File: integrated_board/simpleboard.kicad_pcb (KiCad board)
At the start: 4 copper layers, 50 x 50 mm, 111 parts, among them IC1 MPM36xx, IC2 IP4251, J1 OLED, J2 SERIAL1, J3 USB_B_Micro, J4 Battery, J6 Battery, J8 FAN, J9 Enc, P1 SWD_TC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

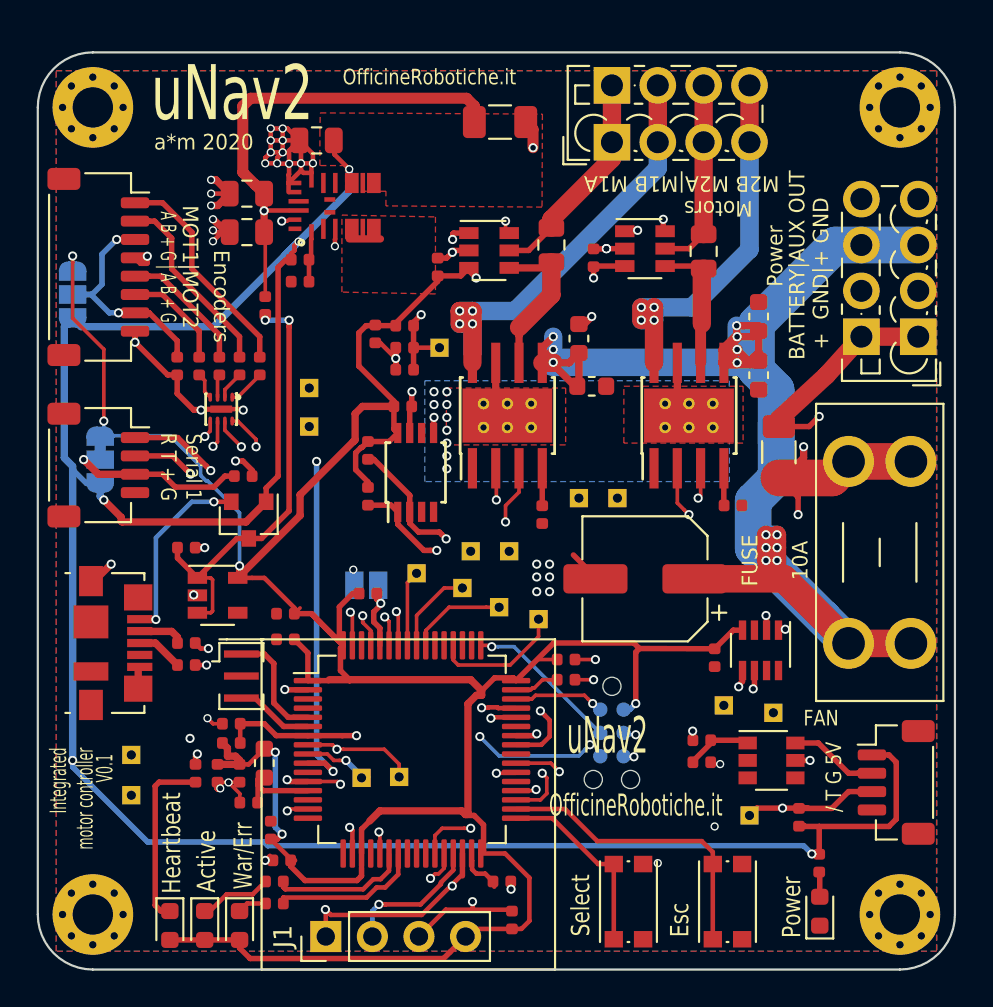
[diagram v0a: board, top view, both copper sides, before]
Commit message: Add supply inversion protection diode, move custom symbol to project lib
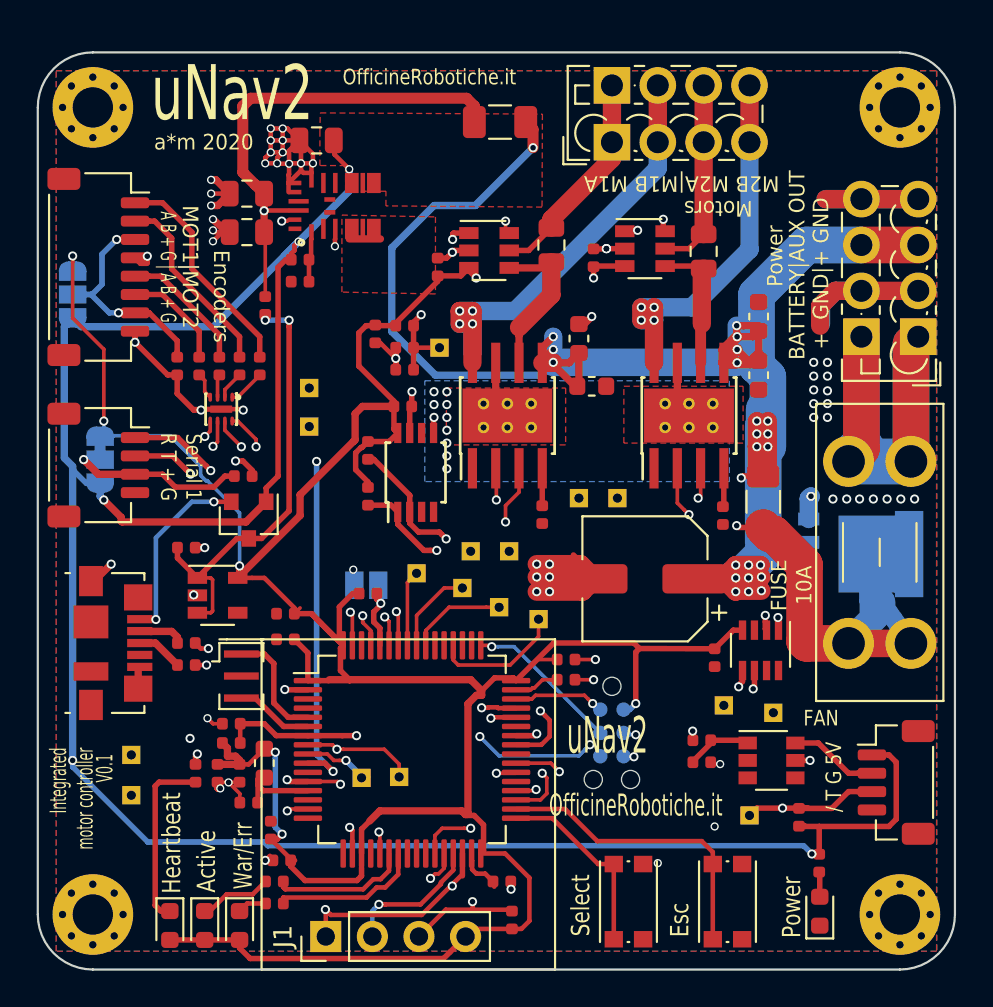
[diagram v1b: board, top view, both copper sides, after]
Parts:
- added D6: D_Schottky_Small, Package_TO_SOT_SMD:LFPAK56, B.Cu at (194.9, 77.3)
- moved R12 2.83 mm to (189.6, 74.5), turned to 270 degrees
- moved R4 0.78 mm to (187.3, 75.2), turned to 270 degrees
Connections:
- F1 pad 1: Net-(F1-Pad1) -> /BATTERY+
- F1 pad 2: VBATT -> Net-(D6-Pad5)
- F2 pad 2: Net-(F1-Pad1) -> VBATT
- R12 pad 1: Net-(F1-Pad1) -> VBATT
- R12 pad 2: /BATTERY+ -> Net-(D6-Pad5)
- U2 pad 1: /BATTERY+ -> Net-(D6-Pad5)
- U2 pad 2: Net-(F1-Pad1) -> VBATT
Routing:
- net Net-(F1-Pad1): track 47.0 -> 0.00 mm, vias 4 -> 0
- net Net-(D6-Pad5): track 0.00 -> 35.6 mm, vias 0 -> 2
- net VBATT: track 94.0 -> 128.0 mm, vias 13 -> 25
- net GND: track 85.9 -> 117.9 mm, vias 66 -> 84
- net /BATTERY+: track 25.1 -> 33.2 mm, vias 2 -> 0

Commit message: Beta 1  (move fan tach pin to a timer input)
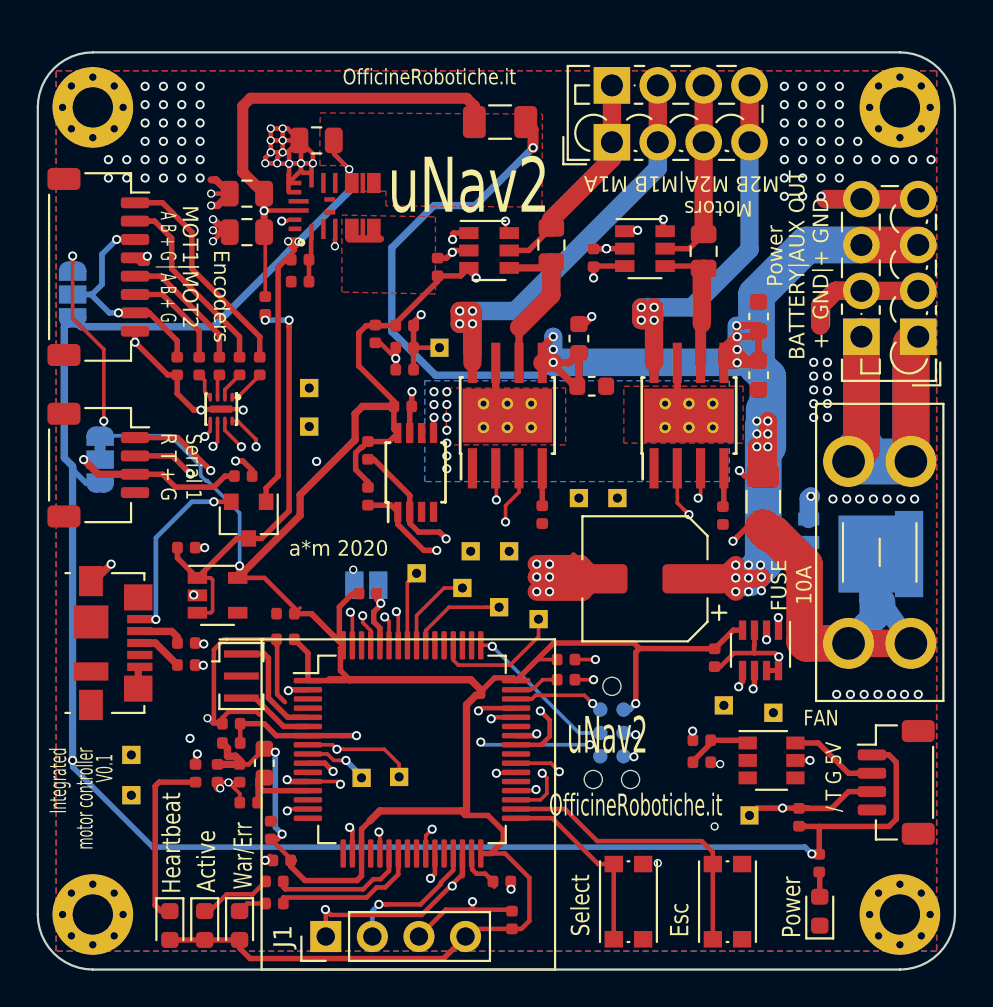
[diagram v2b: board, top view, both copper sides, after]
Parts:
- C28, C29, C3, C8, C9: value C -> 100nF
- D5: value White -> green
- D6: value D_Schottky_Small -> STPS3045DJF
- L1: value L_Small -> bead
- Q1: value Q_DUAL_NMOS_G1S2G2D2S1D1 -> FDC6401N
- R1, R2: value R -> 1k
- R12: value 0.01 -> 0.001
- R15, R16: value 10K -> 10k
- R18, R19, R20, R21: value 1K -> 1k
- R3, R4: value R -> 15k
- R5, R6: value R -> 0.003
- U4: value AP2121AK-3.3 -> AP2112K-3.3
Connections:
- J8 pad 3: /I_FAN_INDEX -> /TIM_FAN_INDEX
- R10 pad 1: /I_FAN_INDEX -> /TIM_FAN_INDEX
- TP10 pad 1: /I_FAN_INDEX -> /TIM_FAN_INDEX
- U5 pad 26: (no net) -> /TIM_FAN_PWM
- U5 pad 27: /TIM_FAN_PWM -> /TIM_FAN_INDEX
- U5 pad 28: /I_FAN_INDEX -> (no net)
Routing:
- net /I_FAN_INDEX: track 30.3 -> 0.00 mm, vias 2 -> 0
- net /TIM_FAN_INDEX: track 0.00 -> 30.0 mm, vias 0 -> 2
- net VBATT: track 128.0 -> 157.4 mm
- net GND: track 117.9 -> 139.2 mm, vias 84 -> 152
- net +5V: track 128.9 -> 120.0 mm
- net Net-(D6-Pad5): track 35.6 -> 37.4 mm
- net +3V3: track 180.6 -> 182.3 mm
- net /I2C_SCL: track 64.6 -> 65.5 mm
- net /TIM_ENC1_B: track 31.0 -> 31.6 mm
- net /NRST: track 24.6 -> 24.1 mm

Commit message: Fixes for #1, #3, #4 & #6
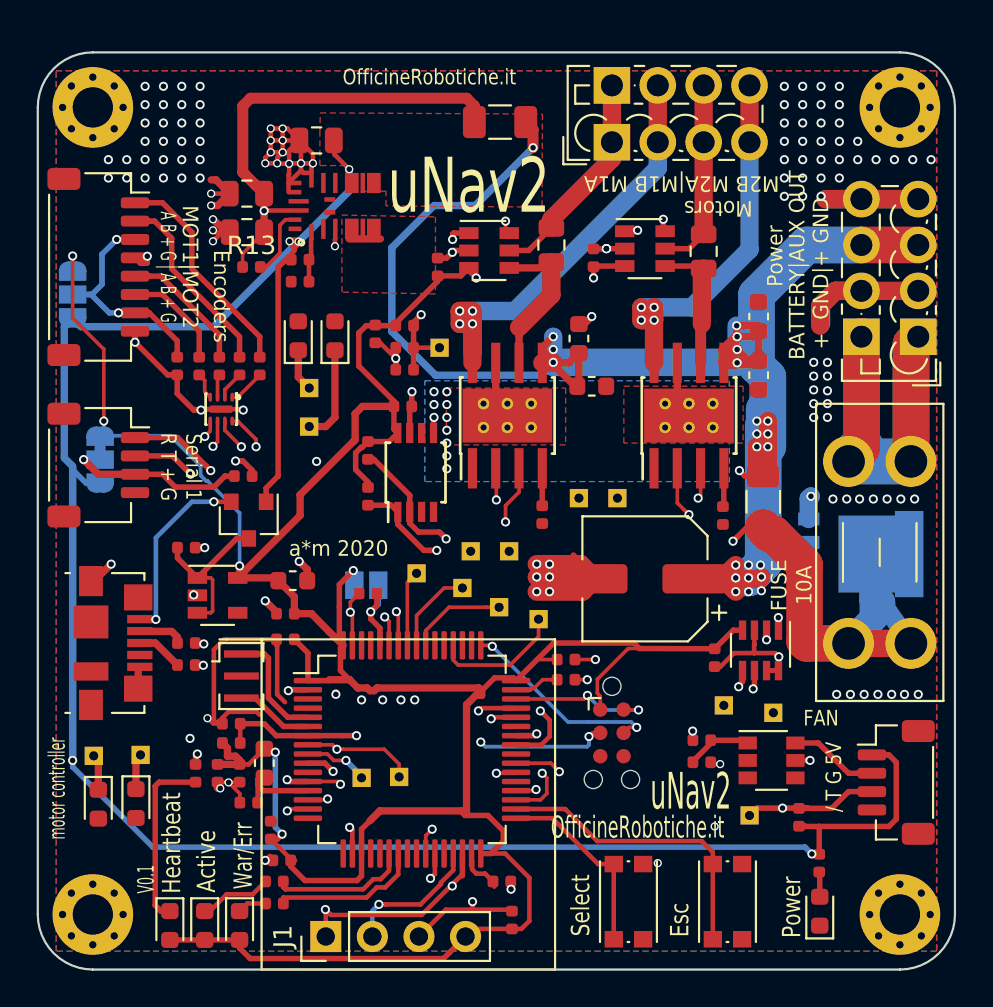
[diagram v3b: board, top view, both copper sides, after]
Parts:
- added C30: 1uF 6.3V, Capacitor_SMD:C_0603_1608Metric, F.Cu at (163.9, 78.8)
- added D10: 3.3V, Diode_SMD:D_0603_1608Metric, F.Cu at (166.2, 65.5)
- added D7: 3.3V, Diode_SMD:D_0603_1608Metric, F.Cu at (155.3, 91.0)
- added D8: 3.3V, Diode_SMD:D_0603_1608Metric, F.Cu at (153.3, 91.0)
- added D9: 3.3V, Diode_SMD:D_0603_1608Metric, F.Cu at (164.2, 65.5)
- C11, C12, C25, C27, C4: value 1uF -> 1uF 10V
- C13, C14, C19, C21, C22, C23, C24, C26, C28, C29, C3, C8, C9: value 100nF -> 100nF 16V
- C15, C16: value 100n -> 100nF 16V
- C17: value 4.7uf -> 22uF 25V
- C18: value 4.7uf -> 4.7uf 25V
- C2, C5: value 1uF -> 1uF 25V
- C20: value 22uf -> 22uf 6.3V
- C6, C7: value 100nF -> 1uF 25V
- P1: moved to F.Cu
- R15: value 10k -> 100K
- R16: value 10k -> 19.1K
- moved TP7 2.97 mm to (153.1, 88.3)
- moved R13 2.23 mm to (161.7, 61.7), turned to 0 degrees
- moved TP5 0.50 mm to (155.6, 88.3)
- turned R8 to 180 degrees
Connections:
- IC1 pad 17: /O_REG_EN -> Net-(IC1-Pad17)
- JP1 pad 1: GND -> +3V3
- R13 pad 1: Net-(C19-Pad1) -> /V_BATT_INT
- R13 pad 2: /V_BATT_INT -> Net-(IC1-Pad17)
- R8 pad 1: +3V3 -> /BOOT0
- R8 pad 2: /BOOT0 -> GND
- U5 pad 14: (no net) -> /TIM_ENC2_A
- U5 pad 21: /TIM_ENC2_A -> (no net)
- U5 pad 61: /O_REG_EN -> (no net)
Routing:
- net /O_REG_EN: track 28.3 -> 0.00 mm, vias 2 -> 0
- net Net-(C19-Pad1): track 24.1 -> 9.23 mm, vias 2 -> 0
- net /TIM_ENC1_A: track 30.3 -> 35.5 mm
- net Net-(IC1-Pad17): track 0.00 -> 3.49 mm
- net /SWDIO: track 5.00 -> 7.91 mm, vias 1 -> 2
- net +3V3: track 182.3 -> 185.1 mm
- net /SWCK: track 8.49 -> 11.2 mm, vias 1 -> 2
- net GND: track 139.2 -> 141.6 mm, vias 152 -> 157
- net /TIM_ENC1_B: track 31.6 -> 33.9 mm
- net /NRST: track 24.1 -> 21.8 mm, vias 4 -> 3
- net /TIM_ENC2_B: track 31.6 -> 33.1 mm
- net /BOOT0: track 4.26 -> 5.50 mm
- net /V_BATT_INT: track 26.1 -> 25.0 mm
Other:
- board text added: "motor controller"
- board text removed: "Integrated motor controller"

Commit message: Additional fixes
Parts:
- removed TP10: TestPoint, TestPoint:TestPoint_THTPad_1.0x1.0mm_Drill0.5mm
- added D11: D_Zener, Diode_SMD:D_0603_1608Metric, F.Cu at (188.2, 91.2)
- added R28: 1k, Resistor_SMD:R_0402_1005Metric, F.Cu at (190.3, 91.8)
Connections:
- J8 pad 3: /TIM_FAN_INDEX -> /Sheet5E8941DD/FAN_TACH
- R10 pad 1: /TIM_FAN_INDEX -> /Sheet5E8941DD/FAN_TACH
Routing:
- net /TIM_FAN_INDEX: track 30.0 -> 22.7 mm
- net /Sheet5E8941DD/FAN_TACH: track 0.00 -> 5.52 mm
- net GND: track 141.6 -> 142.4 mm, vias 157 -> 158

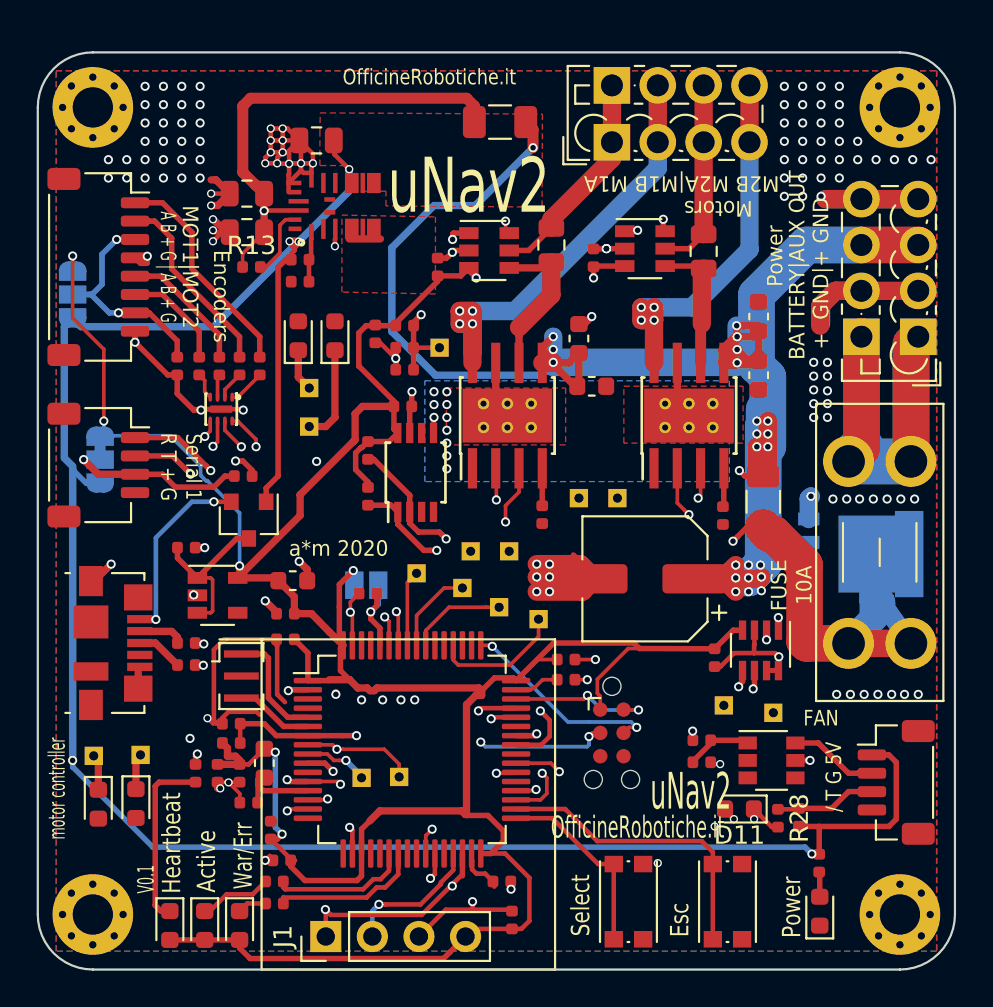
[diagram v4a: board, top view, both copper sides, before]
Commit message: V 0.3: - use a 6 pins connector for each motor - use vertical connectors for usb and serial - additional jst/sh for swt in the back of the board - additional stitching on ground plane
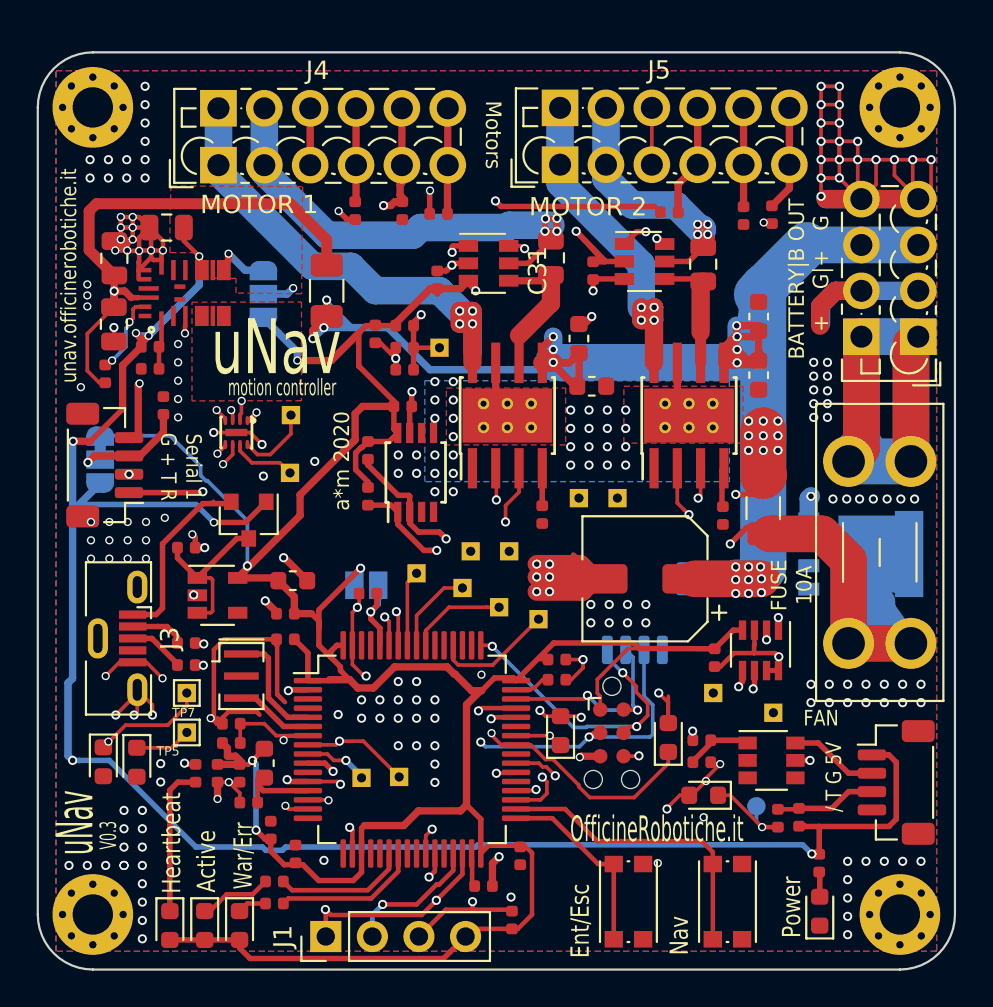
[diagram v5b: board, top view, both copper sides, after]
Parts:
- removed J9: Enc, Connector_JST:JST_SH_SM08B-SRSS-TB_1x08-1MP_P1.00mm_Horizontal
- added C31: 100nF 16V, Capacitor_SMD:C_0402_1005Metric, F.Cu at (169.9, 58.6)
- added C32: 100nF 16V, Capacitor_SMD:C_0402_1005Metric, F.Cu at (176.3, 93.8)
- added J5: Motor2, TerminalBlock_Phoenix:TerminalBlock_Phoenix_PTSM-0,5-6-2.5-V-THR_1x06_P2.50mm_Vertical, F.Cu at (178.5, 56.1)
- added J7: SWD2, Connector_JST:JST_SH_SM04B-SRSS-TB_1x04-1MP_P1.00mm_Horizontal, B.Cu at (182.6, 80.6)
- added TP10: TestPoint, TestPoint:TestPoint_THTPad_1.0x1.0mm_Drill0.5mm, B.Cu at (189.2, 91.1)
- J2: footprint Connector_JST:JST_SH_SM04B-SRSS-TB_1x04-1MP_P1.00mm_Horizontal -> Connector_JST:JST_SH_BM04B-SRSS-TB_1x04-1MP_P1.00mm_Vertical
- J3: footprint Connector_USB:USB_Micro-B_Molex_47346-0001 -> Connector_USB:USB_Micro-B_Molex-105133-0001
- J4: value Battery -> Motor1; footprint TerminalBlock_Phoenix:TerminalBlock_Phoenix_PTSM-0,5-4-2.5-V-THR_1x04_P2.50mm_Vertical -> TerminalBlock_Phoenix:TerminalBlock_Phoenix_PTSM-0,5-6-2.5-V-THR_1x06_P2.50mm_Vertical
- TP5, TP7: moved to F.Cu
- moved R21 32.3 mm to (190.0, 58.9)
- moved C3 31.9 mm to (188.5, 58.9), turned to 90 degrees
- moved D10 28.5 mm to (184.4, 87.3)
- moved R19 25.9 mm to (184.4, 58.7), turned to 180 degrees
- moved D9 25.8 mm to (178.5, 87.0)
- moved J4 21.5 mm to (159.8, 56.1)
- moved R20 13.7 mm to (171.8, 58.8), turned to 180 degrees
- moved F2 13.2 mm to (165.8, 63.0), turned to 270 degrees
- moved JP3 10.4 mm to (162.3, 63.2), turned to 90 degrees
- moved R18 9.94 mm to (167.3, 58.6)
- moved R13 9.88 mm to (153.7, 67.5), turned to 90 degrees
- moved IC1 9.45 mm to (158.3, 63.1)
- moved R15 9.45 mm to (156.1, 66.0)
- moved R16 9.45 mm to (156.1, 67.2)
- moved C20 9.45 mm to (157.0, 59.5)
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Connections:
- C3 pad 1: /Sheet5E8E545F/ENC_Power -> GND
- C3 pad 2: GND -> /Sheet5E8E545F/ENC_Power
- J2 pad MP: (no net) -> GND
- J4 pad 1: /Sheet5E94E0E4/MOT1_A -> /Sheet5E94E0E4/MOT1_B
- J4 pad 2: /Sheet5E94E0E4/MOT1_B -> /Sheet5E94E0E4/MOT1_A
- J4 pad 3: /Sheet5E94E0E4/MOT2_A -> GND
- J4 pad 4: /Sheet5E94E0E4/MOT2_B -> /Sheet5E8E545F/ENC1_A
- P1 pad 6: (no net) -> /SPI1_SCK
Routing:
- net GND: track 142.4 -> 221.2 mm, vias 158 -> 231
- net Net-(IC2-Pad5): track 1.46 -> 39.9 mm, vias 0 -> 2
- net Net-(IC2-Pad6): track 1.26 -> 31.3 mm, vias 0 -> 2
- net VBATT: track 157.4 -> 127.7 mm, vias 25 -> 30
- net /Sheet5E8E545F/ENC_Power: track 13.2 -> 42.4 mm
- net Net-(IC2-Pad7): track 1.55 -> 21.7 mm, vias 0 -> 2
- net /Sheet5E94E0E4/MOT1_A: track 11.9 -> 30.6 mm, vias 0 -> 4
- net +5V: track 119.7 -> 105.3 mm, vias 5 -> 8
- net Net-(IC2-Pad8): track 2.01 -> 14.6 mm, vias 0 -> 2
- net /SPI1_SCK: track 5.33 -> 17.6 mm, vias 0 -> 1
- net /NRST: track 21.8 -> 32.9 mm
- net /BATTERY+: track 33.2 -> 41.6 mm
- net /Sheet5E94E0E4/MOT2_A: track 10.5 -> 17.6 mm, vias 0 -> 4
- net /TIM_ENC1_B: track 33.9 -> 26.8 mm
- net /Sheet5E8E545F/ENC1_A: track 12.1 -> 5.11 mm
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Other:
- board text added: "+ G|+ G"
- board text added: "BATTERY|B OUT"
- board text added: "ENCB VCC ENCA G | M+ M-"
- board text added: "EncB VCC EncA G | M+ M-"
- board text added: "Ent/Esc"
- board text added: "G NRST SWDIO SWDCLK"
- board text added: "GND OUT+ GND BATTERY IN+"
- board text added: "MOTOR 1"
- board text added: "MOTOR 2"
- board text added: "Nav"
- board text added: "Serial 1 G + T R"
- board text added: "V0.3"
- board text added: "alessiomorale.com/t/unav"
- board text added: "motion controller"
- board text added: "uNav"
- board text added: "unav.officinerobotiche.it"
- board text removed: "+ GND|+ GND"
- board text removed: "A B + G | A B + G"
- board text removed: "BATTERY|AUX OUT"
- board text removed: "Encoders"
- board text removed: "Esc"
- board text removed: "M2B M2A|M1B M1A"
- board text removed: "MOT1|MOT2"
- board text removed: "Select"
- board text removed: "Serial 1 R T + G"
- board text removed: "V0.1"
- board text removed: "motor controller"
- board text removed: "uNav2"
